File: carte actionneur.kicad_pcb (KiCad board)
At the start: 2 copper layers, 87.5 x 90 mm, 92 parts, among them IC1 LMR51460SQDRRRQ1, IC2 LMR51460SQDRRRQ1, J1 Conn_01x08_Pin, J10 Conn_01x08_Pin, J11 Conn_01x04_Pin, J12 Conn_01x09_Pin, J17 Conn_01x04_Pin, J2 Conn_01x02, J3 Conn_01x04_Pin, J5 Conn_01x03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

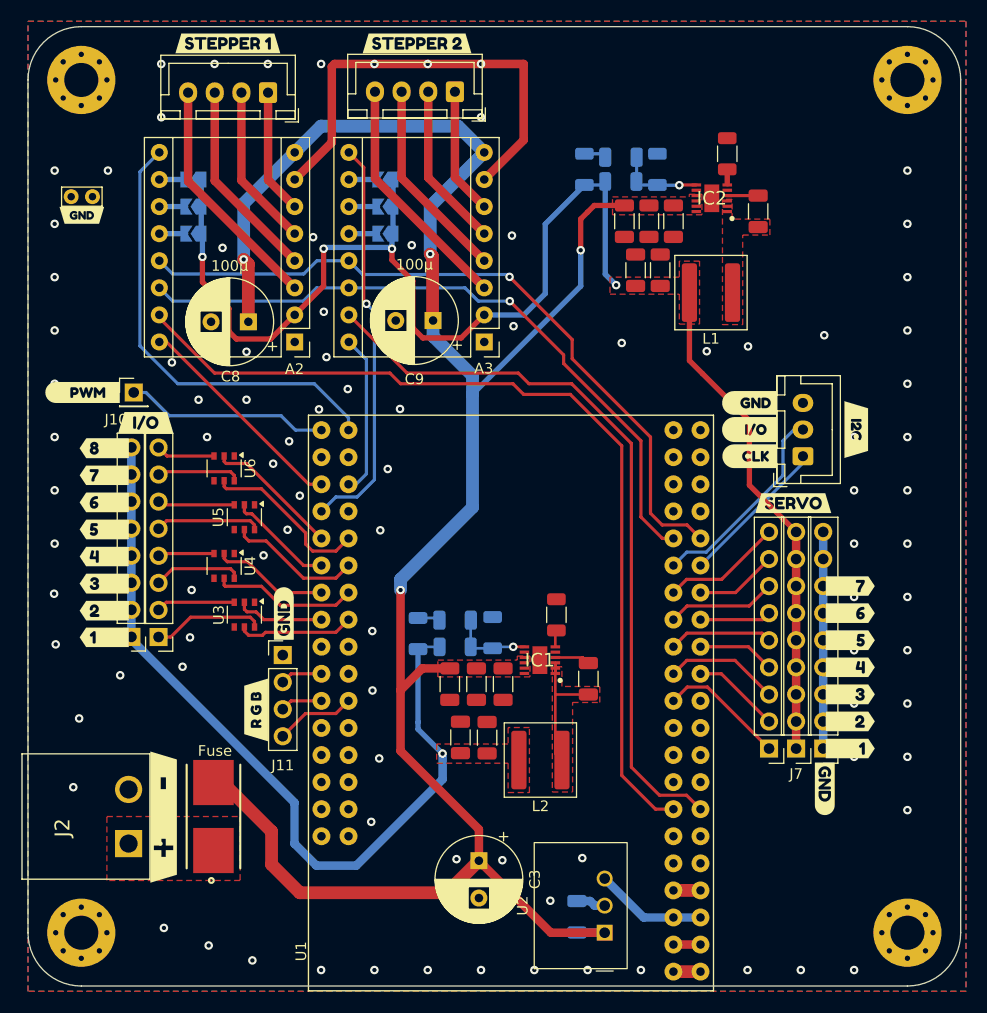
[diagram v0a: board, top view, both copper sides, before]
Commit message: - Added 3 servo pin, for a total of 12 // - Modified pin assignment to connect to proper PWM arduino pins // - Added pull-down resistors to mosfets // - Deleted PWM lidar pin // - Modified inductor components to fit under the arduino
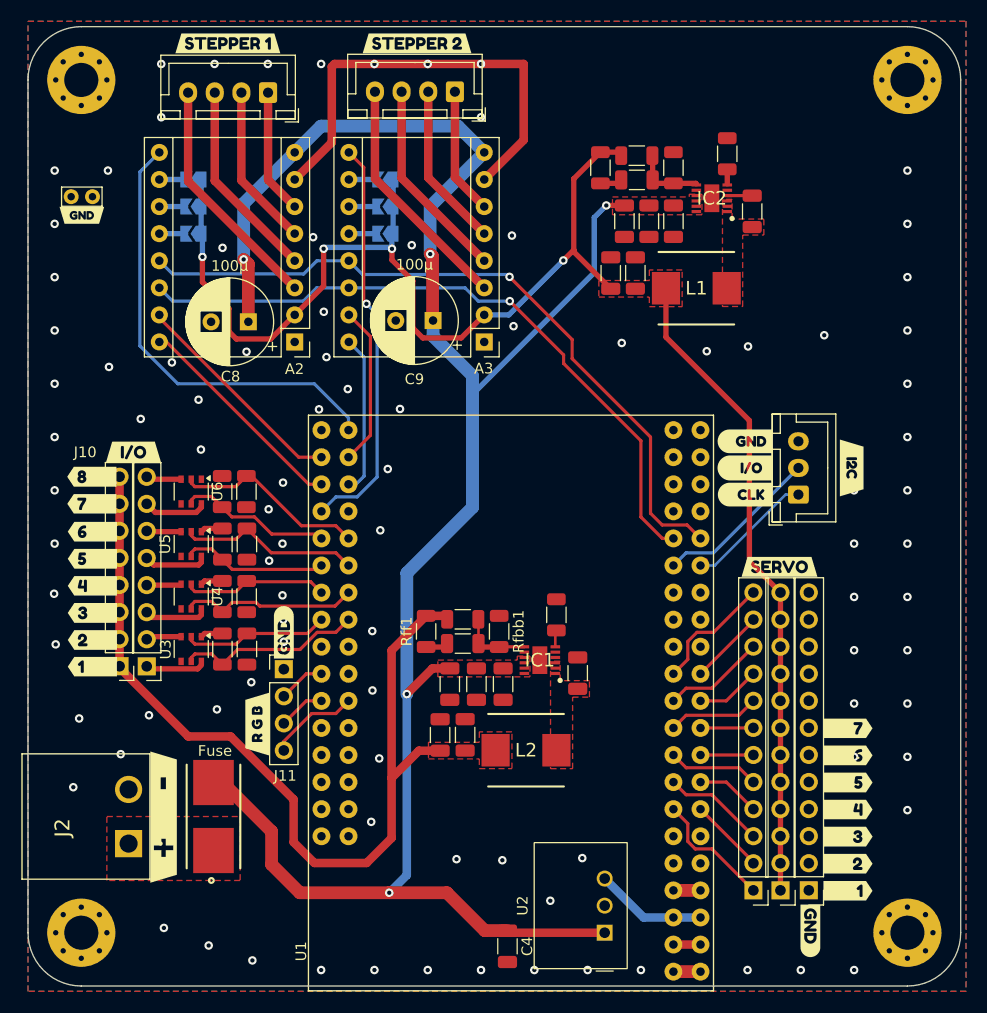
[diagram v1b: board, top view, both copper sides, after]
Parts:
- removed C3: 100µ, Capacitor_THT:CP_Radial_D8.0mm_P3.50mm
- removed J9: Conn_01x01_Pin, Connector_PinHeader_2.54mm:PinHeader_1x01_P2.54mm_Vertical
- removed kibuzzard-67A14A78: G***, kibuzzard-67A14A78
- added R1: 1k, Resistor_SMD:R_1206_3216Metric, F.Cu at (132.5, 107.9)
- added R2: 1k, Resistor_SMD:R_1206_3216Metric, F.Cu at (130.2, 107.9)
- added R3: 1k, Resistor_SMD:R_1206_3216Metric, F.Cu at (132.5, 103.0)
- added R4: 1k, Resistor_SMD:R_1206_3216Metric, F.Cu at (130.2, 103.0)
- added R5: 1k, Resistor_SMD:R_1206_3216Metric, F.Cu at (132.5, 93.1)
- added R6: 1k, Resistor_SMD:R_1206_3216Metric, F.Cu at (130.2, 93.1)
- added R7: 1k, Resistor_SMD:R_1206_3216Metric, F.Cu at (130.2, 98.0)
- added R8: 1k, Resistor_SMD:R_1206_3216Metric, F.Cu at (132.5, 98.0)
- C4, Cff1, Cff2, Rfbb1, Rfbb2, Rfbt1, Rfbt2, Rff1, Rff2: moved to F.Cu
- J12, J7, J8: value Conn_01x09_Pin -> Conn_01x12_Pin; footprint Connector_PinHeader_2.54mm:PinHeader_1x09_P2.54mm_Vertical -> Connector_PinHeader_2.54mm:PinHeader_1x12_P2.54mm_Vertical
- L1, L2: footprint Inductor_SMD:L_Coilcraft_XAL6030-XXX -> HCMA0703-8R2-R:INDPM7168X300N
- moved kibuzzard-679EA236 13.4 mm to (185.4, 134.3)
- moved J12 13.4 mm to (180.1, 130.5)
- moved J7 13.4 mm to (182.6, 130.5)
- moved J8 13.4 mm to (185.2, 130.5)
- moved kibuzzard-679EA1D9 13.3 mm to (188.9, 130.6)
- moved kibuzzard-679EA1F0 13.3 mm to (188.9, 128.0)
- moved kibuzzard-679EA1FA 13.3 mm to (188.9, 122.9)
- moved kibuzzard-679EA204 13.3 mm to (188.9, 120.4)
- moved kibuzzard-679EA208 13.3 mm to (188.9, 125.5)
- moved kibuzzard-679EA20F 13.3 mm to (188.9, 117.9)
- moved kibuzzard-679EA213 13.3 mm to (188.9, 115.3)
- moved C4 7.09 mm to (157.0, 135.8), turned to -90 degrees
- moved kibuzzard-679EA25C 6.11 mm to (182.5, 100.2)
- moved U3 5.94 mm to (127.3, 107.9)
- moved U5 5.59 mm to (127.3, 98.0)
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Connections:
- U1 pad D10: Servo1 -> Servo10
- U1 pad D11: unconnected-(U1-PadD11) -> Servo9
- U1 pad D12: Servo3 -> Servo12
- U1 pad D13: Servo2 -> Servo11
- U1 pad D14: Servo5 -> unconnected-(U1-PadD14)
- U1 pad D15: Servo4 -> unconnected-(U1-PadD15)
- U1 pad D16: Servo7 -> unconnected-(U1-PadD16)
- U1 pad D17: Servo6 -> unconnected-(U1-PadD17)
- U1 pad D18: Servo9 -> unconnected-(U1-PadD18)
- U1 pad D19: Servo8 -> unconnected-(U1-PadD19)
- U1 pad D2: STEP1 -> Servo1
- U1 pad D3: STEP2 -> Servo2
- U1 pad D36: Mosfet5 -> Mosfet6
- U1 pad D37: Mosfet6 -> Mosfet5
- U1 pad D38: Mosfet7 -> Mosfet8
- U1 pad D39: Mosfet8 -> Mosfet7
- U1 pad D4: unconnected-(U1-PadD4) -> Servo3
- U1 pad D44: unconnected-(U1-PadD44) -> STEP1
- U1 pad D45: unconnected-(U1-PadD45) -> STEP2
- U1 pad D46: PWM_LIDAR -> unconnected-(U1-PadD46)
- U1 pad D5: unconnected-(U1-PadD5) -> Servo4
- U1 pad D6: unconnected-(U1-PadD6) -> Servo5
- U1 pad D7: unconnected-(U1-PadD7) -> Servo6
- U1 pad D8: unconnected-(U1-PadD8) -> Servo8
- U1 pad D9: unconnected-(U1-PadD9) -> Servo7
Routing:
- net STEP1: track 85.7 -> 20.9 mm
- net STEP2: track 70.0 -> 15.0 mm
- net PWM_LIDAR: track 19.1 -> 0.00 mm
- net GND: track 68.1 -> 51.5 mm, vias 93 -> 95
- net SW: track 13.5 -> 0.00 mm
- net +5V: track 136.8 -> 148.6 mm
- net Servo12: track 0.00 -> 11.6 mm
- net Servo10: track 0.00 -> 9.61 mm
- net +12V: track 76.9 -> 84.9 mm, vias 1 -> 0
- net Mosfet5: track 9.97 -> 17.1 mm
- net Servo11: track 0.00 -> 7.14 mm
- net Mosfet2: track 10.9 -> 17.4 mm
- net +BATT: track 194.1 -> 188.3 mm, vias 4 -> 5
- net Mosfet7: track 12.6 -> 18.1 mm
- net Mosfet1: track 8.29 -> 13.7 mm
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
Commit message: Added TCA9548A module for I2C multiplexing
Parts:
- removed J11: Conn_01x04_Pin, Connector_PinHeader_2.54mm:PinHeader_1x04_P2.54mm_Vertical
- removed kibuzzard-679EA213: G***, kibuzzard-679EA213
- removed kibuzzard-67A0E12F: G***, kibuzzard-67A0E12F
- added J4: Conn_01x03, Connector_JST:JST_XH_B3B-XH-A_1x03_P2.50mm_Vertical, F.Cu at (193.1, 88.5)
- added J6: Conn_01x03, Connector_JST:JST_XH_B3B-XH-A_1x03_P2.50mm_Vertical, F.Cu at (193.1, 66.1)
- added J9: Conn_01x03, Connector_JST:JST_XH_B3B-XH-A_1x03_P2.50mm_Vertical, F.Cu at (193.1, 77.3)
- added R10: 1k, Resistor_SMD:R_1206_3216Metric, F.Cu at (188.0, 92.8)
- added R11: 1k, Resistor_SMD:R_1206_3216Metric, F.Cu at (188.0, 88.4)
- added R12: 1k, Resistor_SMD:R_1206_3216Metric, F.Cu at (188.0, 86.1)
- added R13: 1k, Resistor_SMD:R_1206_3216Metric, F.Cu at (187.9, 66.0)
- added R14: 1k, Resistor_SMD:R_1206_3216Metric, F.Cu at (187.9, 63.7)
- added R15: 1k, Resistor_SMD:R_1206_3216Metric, F.Cu at (188.0, 77.2)
- added R16: 1k, Resistor_SMD:R_1206_3216Metric, F.Cu at (188.0, 74.9)
- added R9: 1k, Resistor_SMD:R_1206_3216Metric, F.Cu at (188.0, 95.1)
- added U7: TCA9548APWR, Adafruit TCA9548A:ADA Perso, F.Cu at (170.8, 67.9)
- moved Cff2 31.8 mm to (153.8, 91.8)
- moved Chf2 31.8 mm to (157.2, 95.6)
- moved Cin3 31.8 mm to (154.9, 95.6)
- moved IC2 31.8 mm to (160.8, 93.5)
- moved Rfbb2 31.8 mm to (157.2, 90.6)
- moved Rfbt2 31.8 mm to (153.8, 89.5)
- moved C1 31.8 mm to (151.3, 100.5)
- moved C2 31.8 mm to (153.6, 100.5)
- moved Cboot2 31.8 mm to (164.6, 94.7)
- moved Cin4 31.8 mm to (152.6, 95.6)
- moved L1 31.8 mm to (159.3, 101.9)
- moved Rff2 31.8 mm to (150.3, 90.6)
- moved Rt2 31.8 mm to (162.2, 89.3)
- moved J5 10.8 mm to (193.1, 99.7)
- moved kibuzzard-67A0F0A3 10.8 mm to (198.1, 97.2)
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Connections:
- J5 pad 1: SWCLK -> Net-(J5-Pin_1)
- J5 pad 2: SWDIO -> Net-(J5-Pin_2)
- U1 pad A10: LED_G -> unconnected-(U1-PadA10)
- U1 pad A11: LED_R -> unconnected-(U1-PadA11)
- U1 pad A12: LED_B -> unconnected-(U1-PadA12)
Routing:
- net +5VD: track 11.1 -> 115.4 mm, vias 0 -> 4
- net Net-(J9-Pin_1): track 0.00 -> 56.3 mm
- net Net-(J9-Pin_2): track 0.00 -> 53.3 mm
- net Net-(J5-Pin_1): track 0.00 -> 49.7 mm
- net Net-(J6-Pin_1): track 0.00 -> 45.1 mm
- net Net-(J4-Pin_1): track 0.00 -> 45.1 mm
- net Net-(J5-Pin_2): track 0.00 -> 43.4 mm
- net Net-(J6-Pin_2): track 0.00 -> 42.7 mm
- net Net-(J4-Pin_2): track 0.00 -> 38.9 mm
- net +5V: track 148.6 -> 173.2 mm, vias 4 -> 3
- net +BATT: track 188.3 -> 165.6 mm
- net SWCLK: track 13.4 -> 28.2 mm
- net SWDIO: track 16.3 -> 29.7 mm
- net LED_R: track 8.49 -> 0.00 mm
- net LED_G: track 5.11 -> 0.00 mm
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
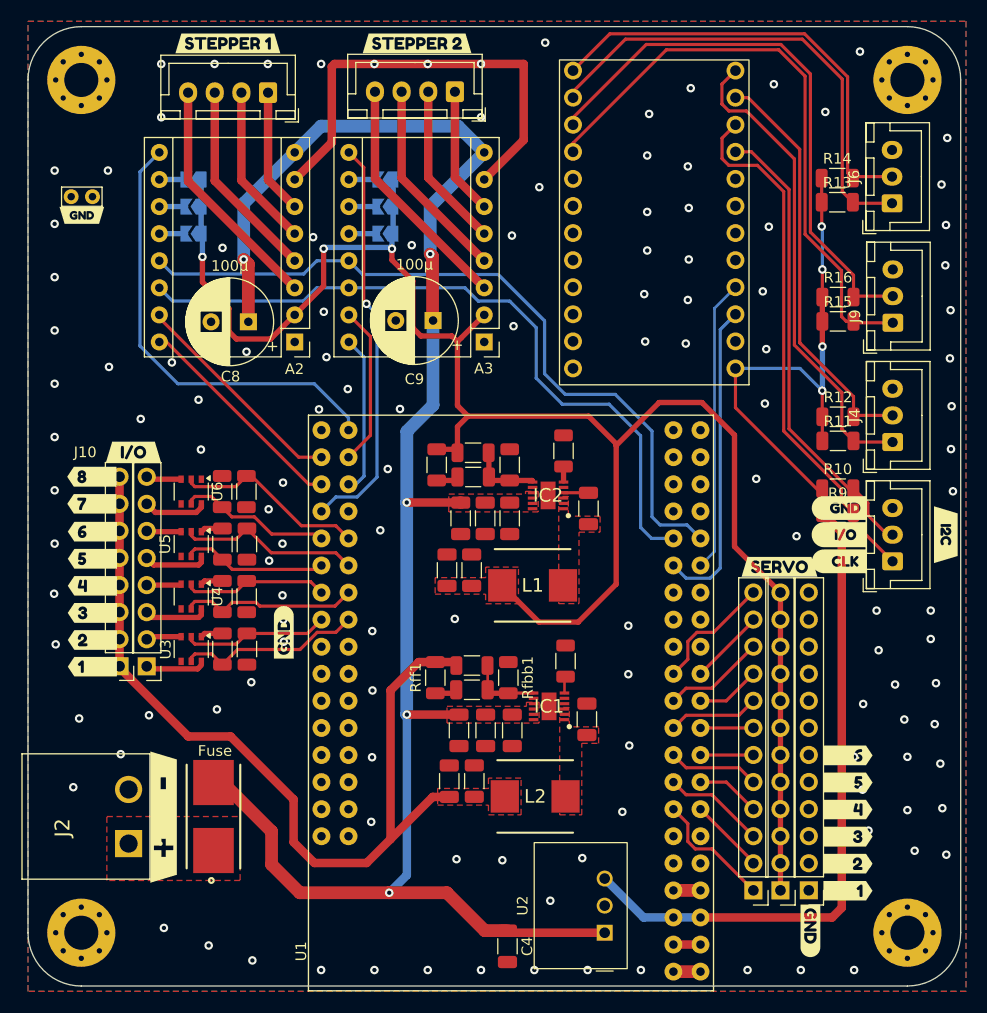
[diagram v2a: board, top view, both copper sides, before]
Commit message: Modified pins and added 5V to I2C
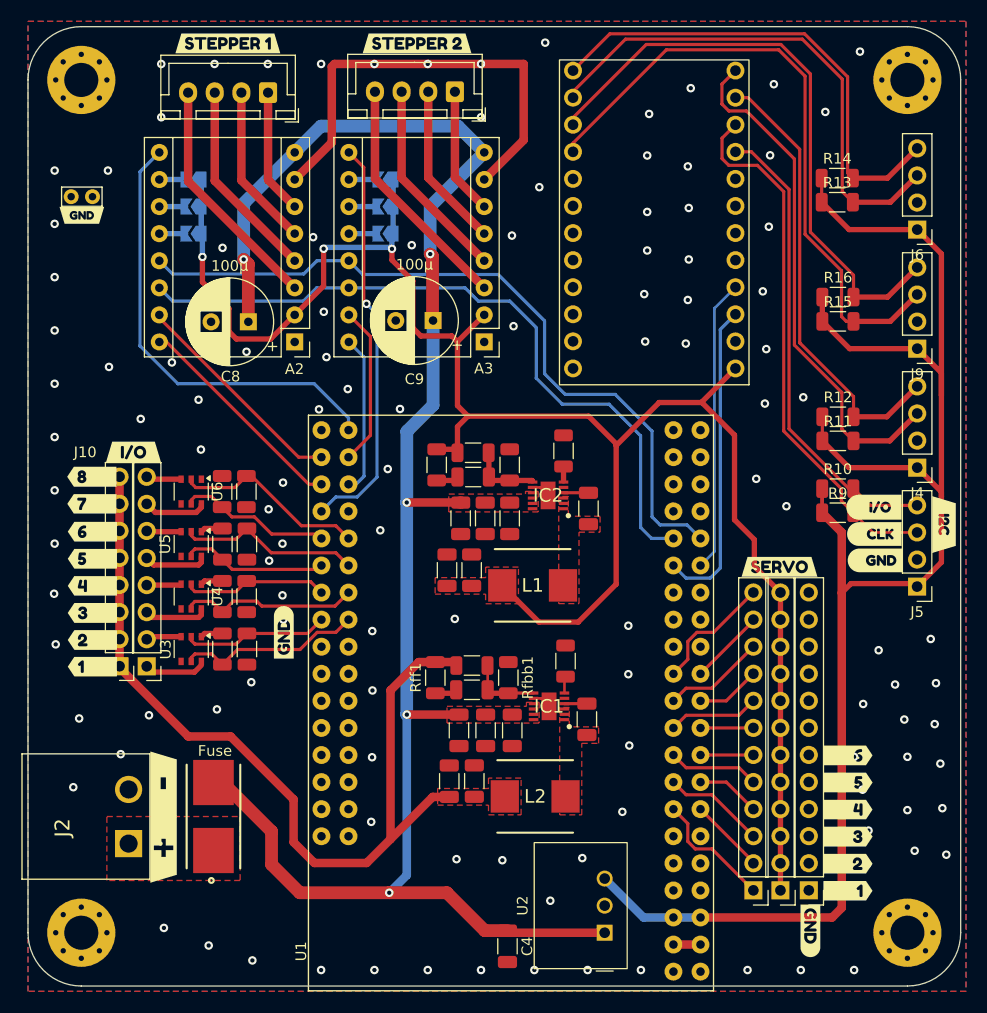
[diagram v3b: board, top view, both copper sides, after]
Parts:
- J4, J5, J6, J9: footprint Connector_JST:JST_XH_B3B-XH-A_1x03_P2.50mm_Vertical -> Connector_PinHeader_2.54mm:PinHeader_1x04_P2.54mm_Vertical
- moved kibuzzard-67A0F0D2 5.96 mm to (191.5, 99.6)
- moved kibuzzard-67A0F0EE 4.17 mm to (191.4, 97.1)
- moved kibuzzard-67A0F0E8 4.15 mm to (191.4, 94.6)
- moved J6 3.42 mm to (195.4, 68.5), turned to 180 degrees
- moved J9 3.34 mm to (195.4, 79.7), turned to 180 degrees
- moved J4 3.33 mm to (195.4, 90.9), turned to 180 degrees
- moved J5 3.31 mm to (195.4, 102.0), turned to 180 degrees
- moved kibuzzard-67A0F0A3 0.97 mm to (197.9, 96.2)
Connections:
- J4 pad 1: Net-(J4-Pin_1) -> +5VD
- J4 pad 2: Net-(J4-Pin_2) -> GND
- J4 pad 3: GND -> Net-(J4-Pin_3)
- J5 pad 1: Net-(J5-Pin_1) -> +5VD
- J5 pad 2: Net-(J5-Pin_2) -> GND
- J5 pad 3: GND -> Net-(J5-Pin_3)
- J6 pad 1: Net-(J6-Pin_1) -> +5VD
- J6 pad 2: Net-(J6-Pin_2) -> GND
- J6 pad 3: GND -> Net-(J6-Pin_3)
- J9 pad 1: Net-(J9-Pin_1) -> +5VD
- J9 pad 2: Net-(J9-Pin_2) -> GND
- J9 pad 3: GND -> Net-(J9-Pin_3)
- R10 pad 2: Net-(J5-Pin_2) -> Net-(J5-Pin_4)
- R11 pad 2: Net-(J4-Pin_1) -> Net-(J4-Pin_3)
- R12 pad 2: Net-(J4-Pin_2) -> Net-(J4-Pin_4)
- R13 pad 2: Net-(J6-Pin_1) -> Net-(J6-Pin_3)
- R14 pad 2: Net-(J6-Pin_2) -> Net-(J6-Pin_4)
- R15 pad 2: Net-(J9-Pin_1) -> Net-(J9-Pin_3)
- R16 pad 2: Net-(J9-Pin_2) -> Net-(J9-Pin_4)
- R9 pad 2: Net-(J5-Pin_1) -> Net-(J5-Pin_3)
- U7 pad 10: Net-(J9-Pin_2) -> Net-(J9-Pin_4)
- U7 pad 11: Net-(J9-Pin_1) -> Net-(J9-Pin_3)
- U7 pad 24: +5VD -> +5V
- U7 pad 4: Net-(J5-Pin_2) -> Net-(J5-Pin_4)
- U7 pad 5: Net-(J5-Pin_1) -> Net-(J5-Pin_3)
- U7 pad 6: Net-(J4-Pin_2) -> Net-(J4-Pin_4)
- U7 pad 7: Net-(J4-Pin_1) -> Net-(J4-Pin_3)
- U7 pad 8: Net-(J6-Pin_2) -> Net-(J6-Pin_4)
- U7 pad 9: Net-(J6-Pin_1) -> Net-(J6-Pin_3)
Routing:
- net Net-(J9-Pin_3): track 0.00 -> 59.9 mm
- net Net-(J9-Pin_4): track 0.00 -> 56.9 mm
- net Net-(J9-Pin_1): track 56.3 -> 0.00 mm
- net Net-(J9-Pin_2): track 53.3 -> 0.00 mm
- net Net-(J5-Pin_3): track 0.00 -> 50.3 mm
- net Net-(J5-Pin_1): track 49.7 -> 0.00 mm
- net Net-(J6-Pin_3): track 0.00 -> 48.6 mm
- net Net-(J4-Pin_3): track 0.00 -> 48.5 mm
- net Net-(J6-Pin_4): track 0.00 -> 46.7 mm
- net Net-(J6-Pin_1): track 45.1 -> 0.00 mm
- net Net-(J4-Pin_1): track 45.1 -> 0.00 mm
- net Net-(J5-Pin_4): track 0.00 -> 43.9 mm
- net Net-(J5-Pin_2): track 43.4 -> 0.00 mm
- net Net-(J4-Pin_4): track 0.00 -> 42.8 mm
- net Net-(J6-Pin_2): track 42.7 -> 0.00 mm
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
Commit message: fix warning pcb
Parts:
- U1: footprint lib-arduino:MODULE_MEGA_PRO_EMBED_CH340G___ATMEGA2560 -> lib-arduino:MODULE_MEGA_PRO_2_CONNECTOR
- moved Rfbb1 0.06 mm to (157.1, 110.6)
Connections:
- U1 pad D28: DIR3 -> unconnected-(U1-PadD28)

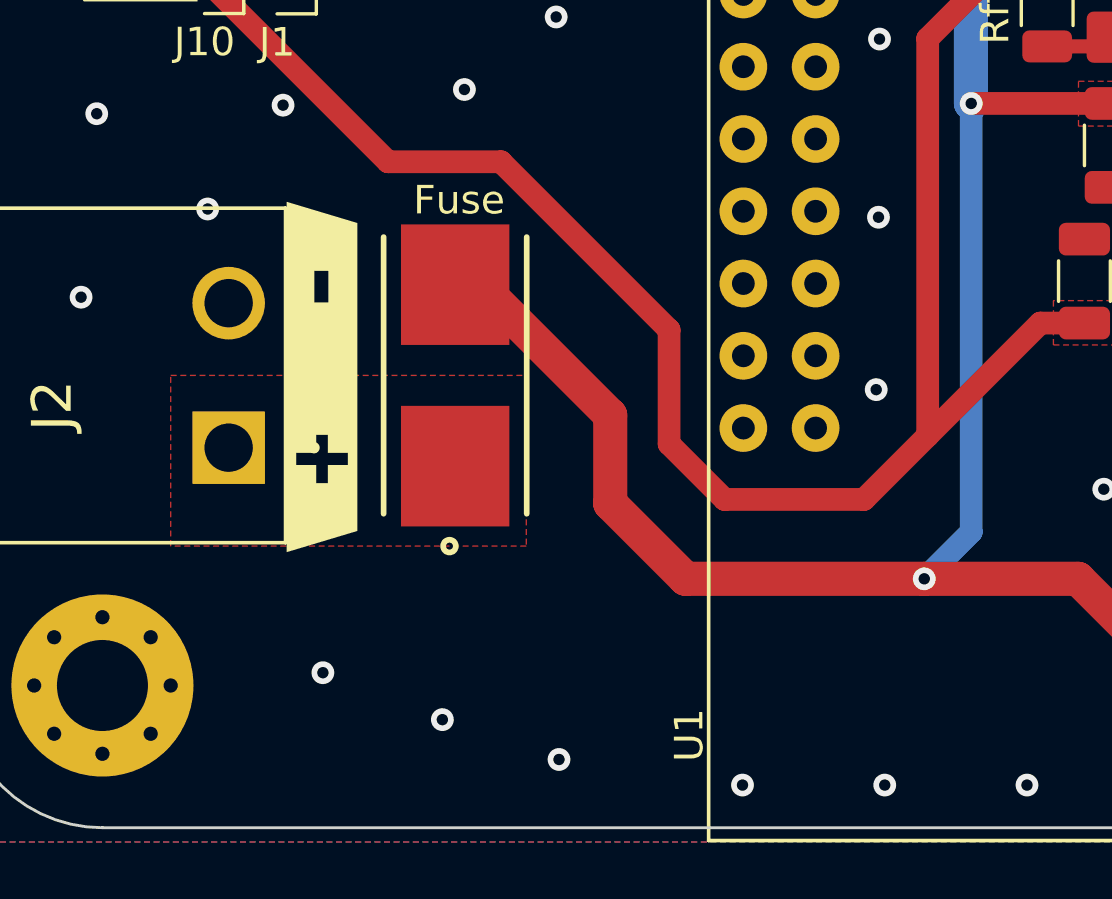
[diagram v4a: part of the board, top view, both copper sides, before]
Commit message: Modified fuse holder footprint
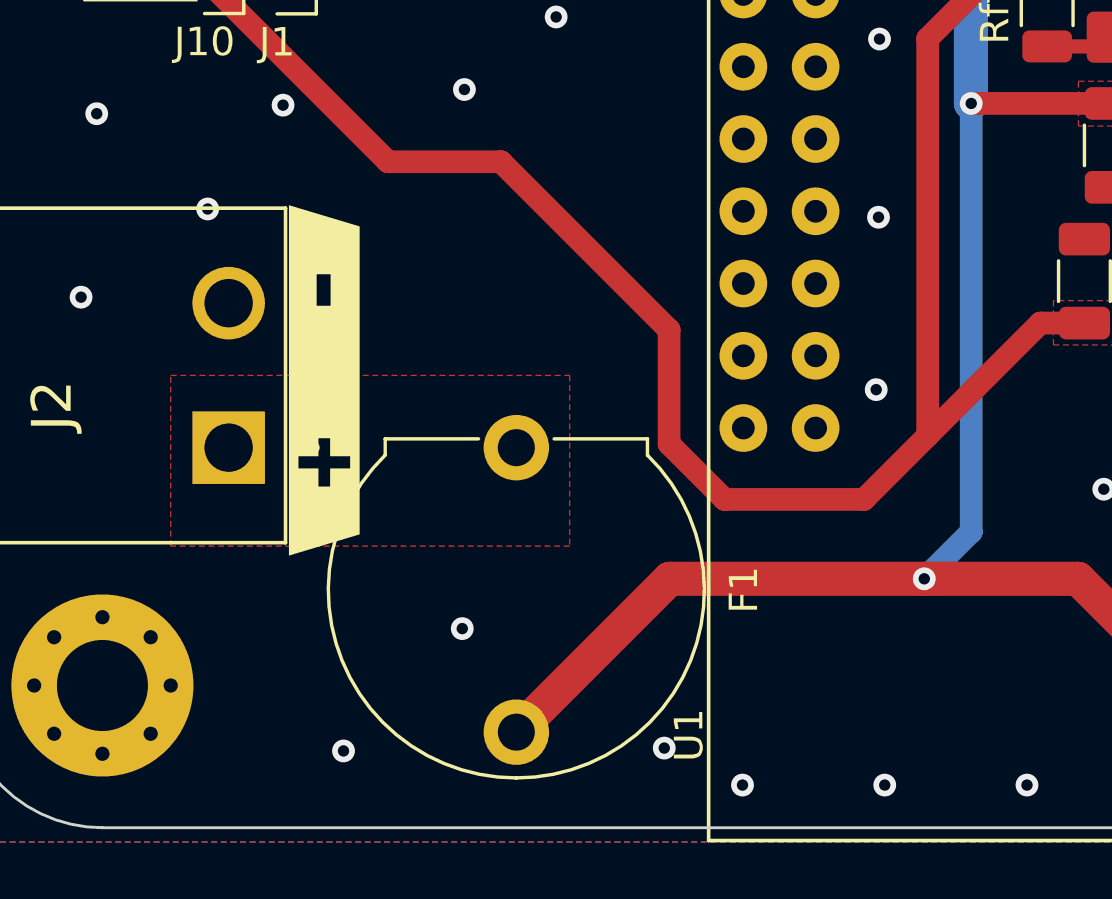
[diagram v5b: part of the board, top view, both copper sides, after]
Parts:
- F1: footprint FuseHolder:FUSE_0154004.DR -> Fuse:Fuseholder_Cylinder-5x20mm_EATON_H15-V-1_Vertical_Closed
- moved F1 3.33 mm to (131.6, 126.1), turned to -90 degrees
- moved kibuzzard-67A13B87 0.14 mm to (124.8, 123.8)
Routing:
- net +BATT: track 165.5 -> 159.5 mm
